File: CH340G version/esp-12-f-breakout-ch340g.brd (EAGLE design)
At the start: 26.7 x 43.3 mm, 22 parts, among them IC1 REG1117, Q1 12.000

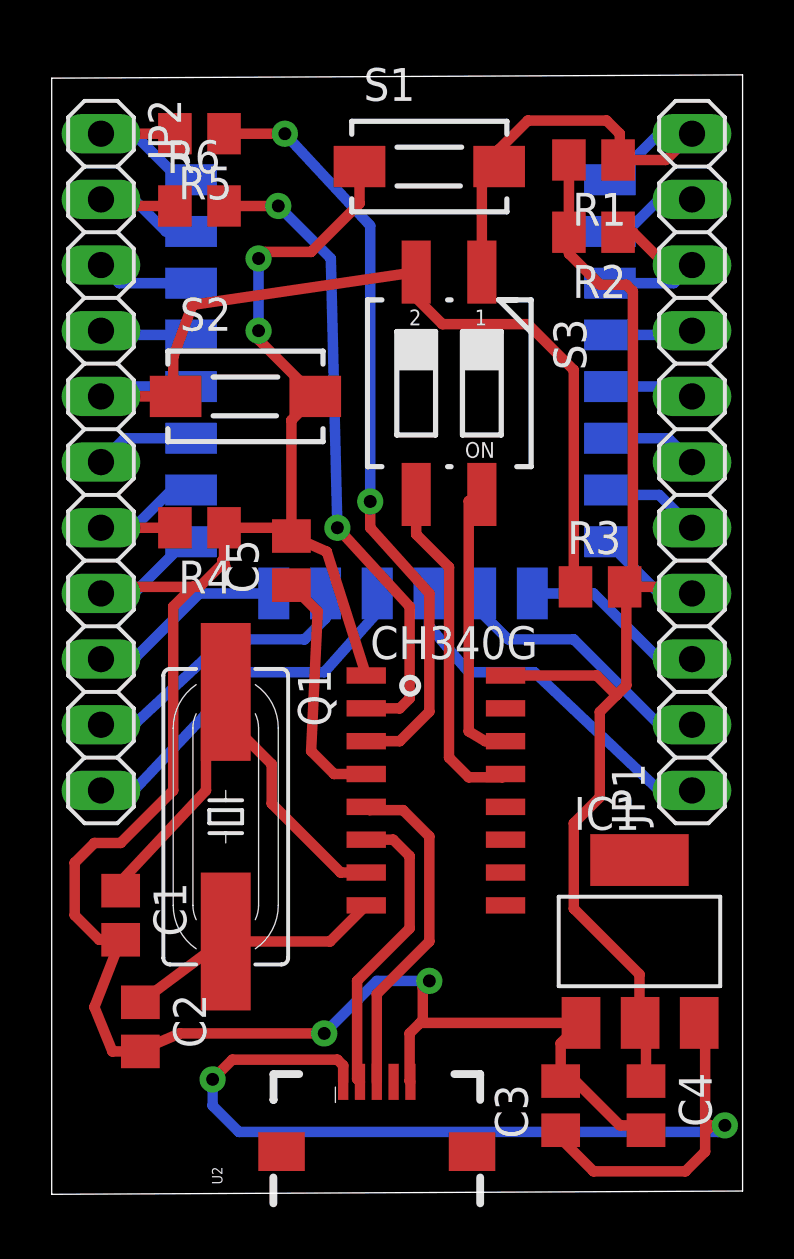
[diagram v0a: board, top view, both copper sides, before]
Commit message: USB +5V pin added to pin headers
- Additional GND pin added
- Stabilizer layout rearranged
- Vias diameter slightly increased
- Drill-aid (0.4 mm) added
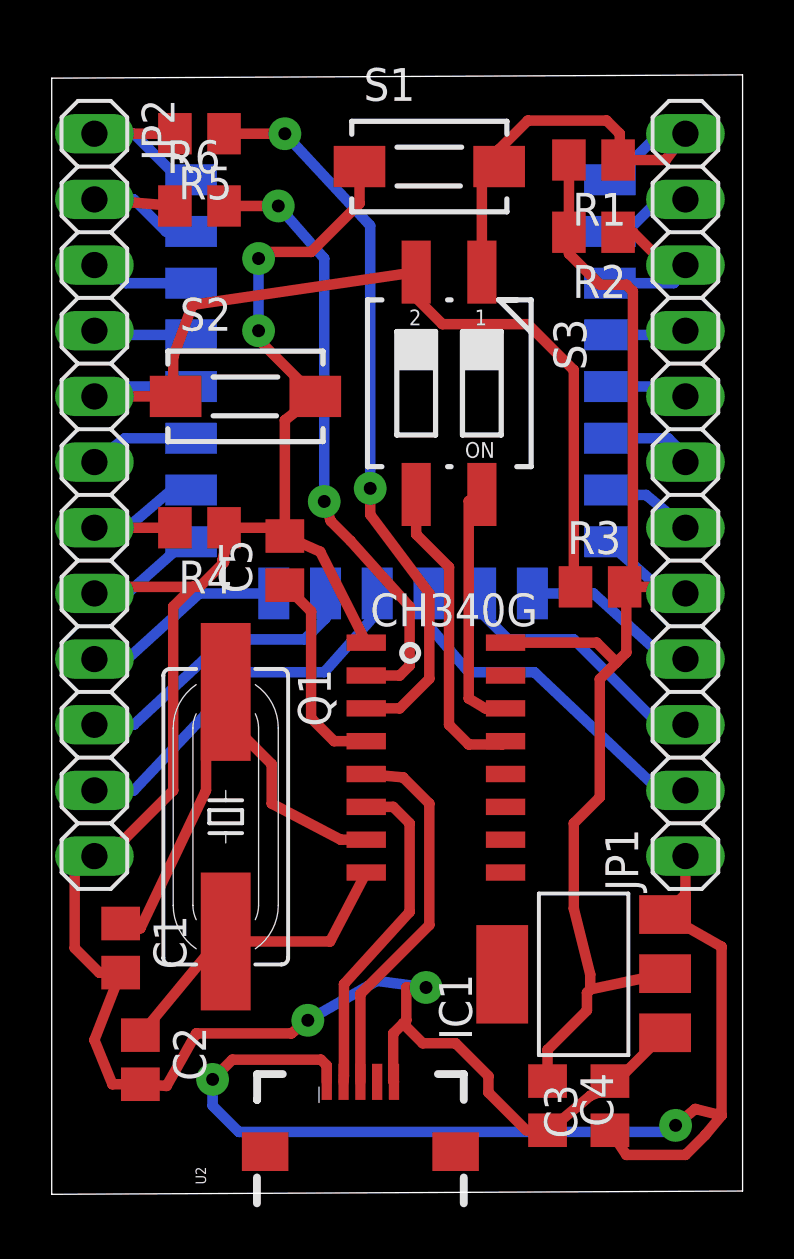
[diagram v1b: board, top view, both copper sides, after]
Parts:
- JP1, JP2: device pinhead:1X11 -> pinhead:1X12
- moved C4 3.81 mm to (18.8, 3.30)
- moved IC1 2.50 mm to (20.2, 8.38), turned to 90 degrees
- moved C3 1.91 mm to (21.2, 3.30)
- moved JP1 1.30 mm to (24.1, 26.9)
- moved JP2 1.30 mm to (1.27, 26.9)
- moved C1 1.27 mm to (2.29, 9.40)
- moved C2 1.27 mm to (3.05, 5.08)
- moved U$2 1.27 mm to (14.5, 16.8)
- moved U2 0.63 mm to (11.6, 1.52)
- moved C5 0.25 mm to (8.64, 24.4)
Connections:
- removed net N$27: C3.1, IC1.3, U2.VBUS1
- new net VUSB: C3.1, IC1.3, JP1.1, U2.VBUS1
- net +3V3: now also JP1.5; no longer JP1.4
- net GND: now also JP2.12
- net N$1: now also JP1.12; no longer JP1.11
- net N$11: now also JP1.3; no longer JP1.2
- net N$15: now also JP1.2; no longer JP1.1
- net N$2: now also JP1.11; no longer JP1.10
- net N$3: now also JP1.10; no longer JP1.9
- net N$4: now also JP1.9; no longer JP1.8
- net N$5: now also JP1.8; no longer JP1.7
- net N$6: now also JP1.7; no longer JP1.6
- net N$7: now also JP1.6; no longer JP1.5
- net N$8: now also JP1.4; no longer JP1.3
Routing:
- net VUSB: track 0.00 -> 44.1 mm, vias 0 -> 2
- net N$27: track 40.1 -> 0.00 mm, vias 2 -> 0
- net GND: track 91.7 -> 94.7 mm
- net +3V3: track 50.8 -> 52.9 mm
- net N$24: track 10.1 -> 12.0 mm
- net N$26: track 13.2 -> 14.7 mm
- net TXD: track 30.2 -> 28.8 mm
- net N$25: track 11.6 -> 12.9 mm
- net RXD: track 24.9 -> 23.6 mm
- net N$9: track 9.34 -> 8.07 mm
- net RESET: track 11.0 -> 9.74 mm
- net GPIO0: track 13.3 -> 12.0 mm
- net N$22: track 7.08 -> 7.59 mm
